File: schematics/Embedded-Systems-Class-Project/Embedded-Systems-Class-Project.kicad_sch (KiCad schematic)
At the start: 6 parts

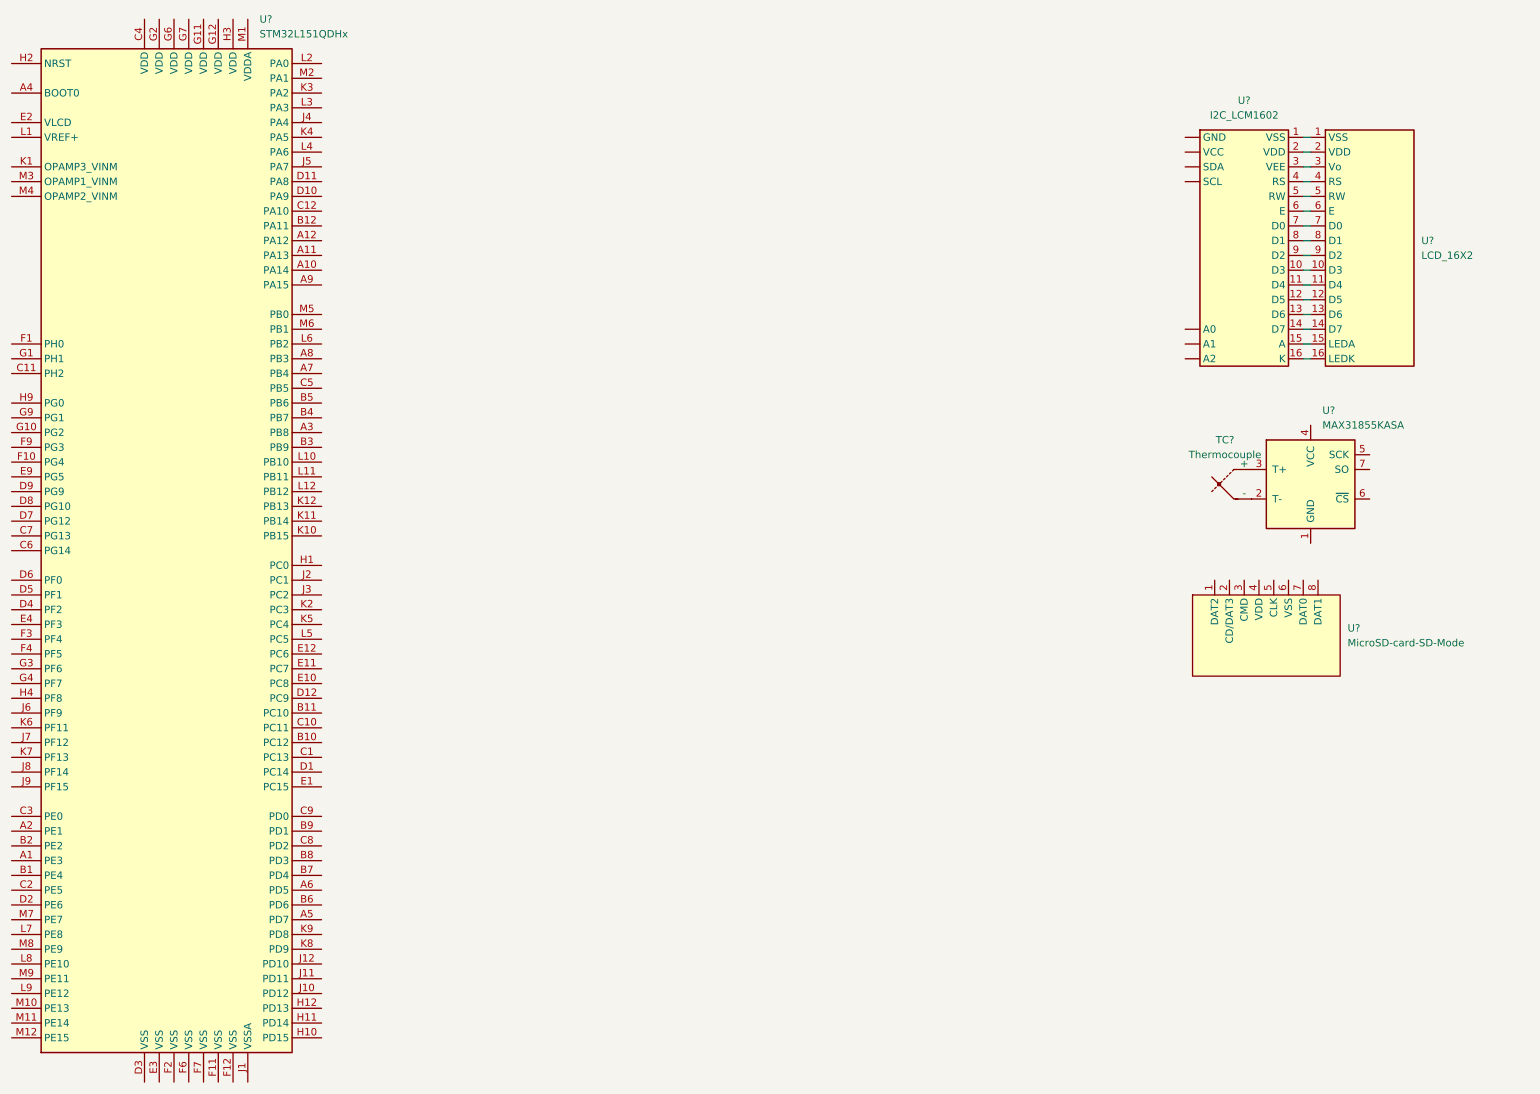
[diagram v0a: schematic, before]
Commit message: added connections to schematic
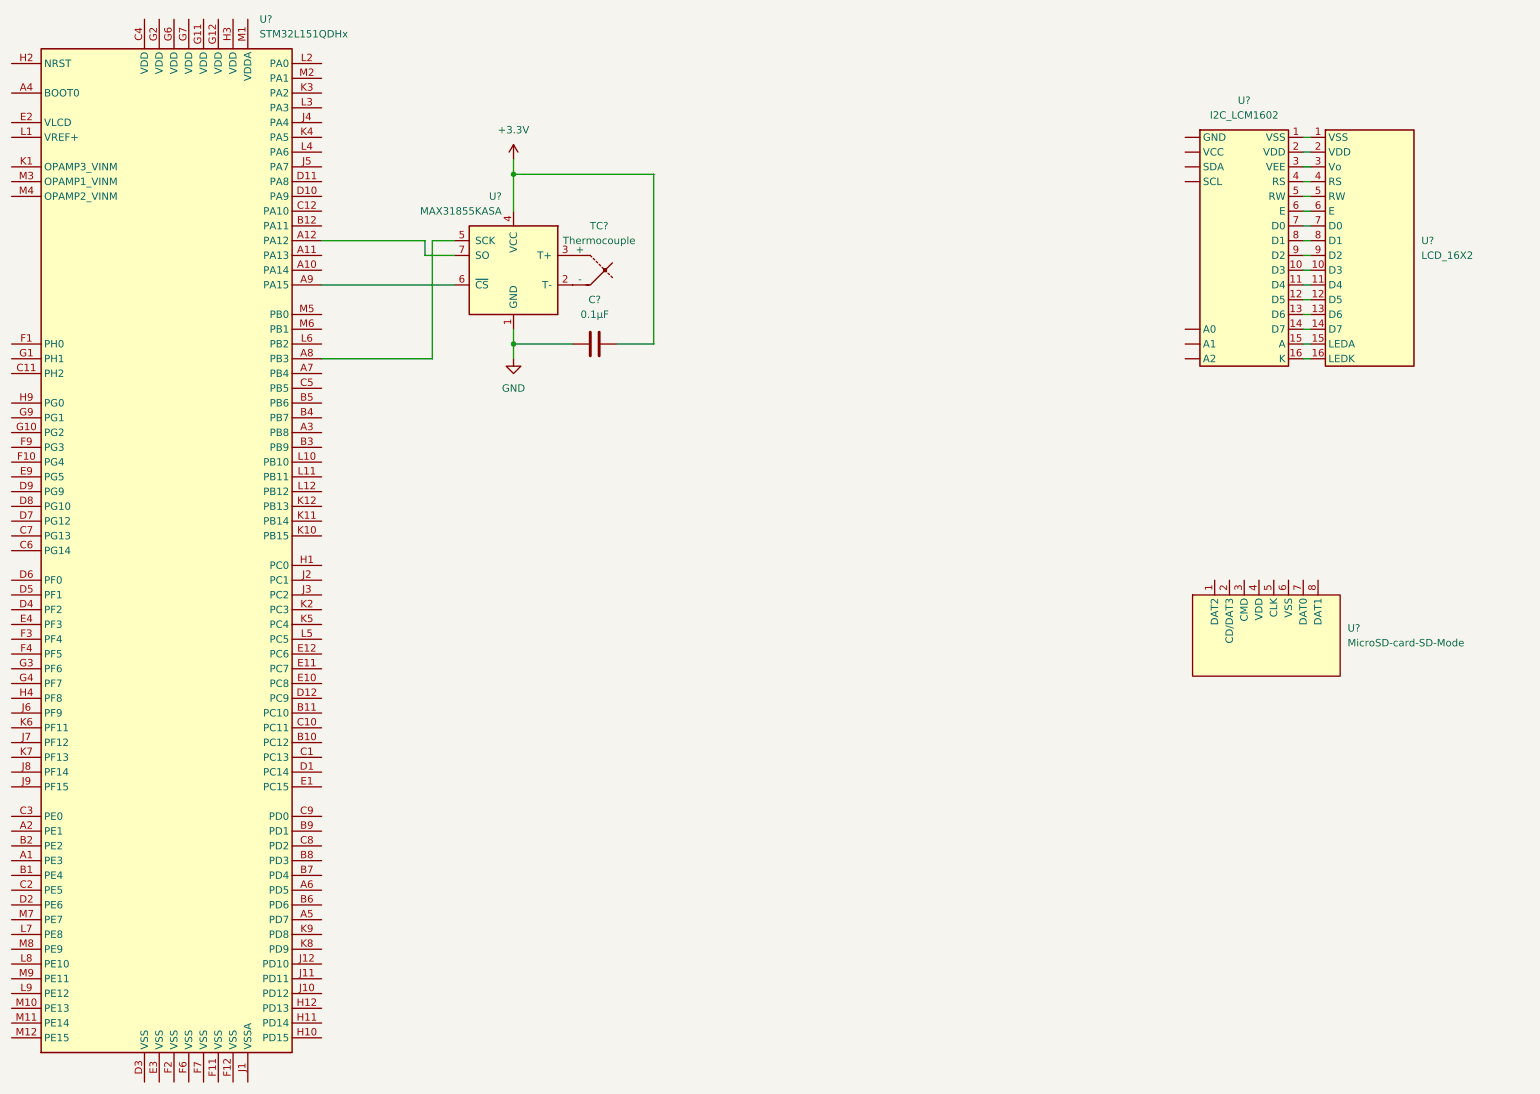
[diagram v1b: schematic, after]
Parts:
- added C?: 0.1μF, symbol Device:C
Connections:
- net GND: now reaches U?.1 (GND)
- net GND: now also C?.2
- net +3.3V: now reaches U?.4 (VCC)
- net +3.3V: now also C?.1
- net at U?.5 (SCK): now also U?.A8 (PB3)
- net at U?.6 (~{CS}): now also U?.A9 (PA15)
- net at U?.7 (SO): now also U?.A12 (PA12)
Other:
- moved on the sheet: TC?, U?
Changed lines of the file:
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@@
 (kicad_sch (version 20211123) (generator eeschema)
   (paper "A4")
+  (junction (at 107.95 39.37) (diameter 0) (color 0 0 0 0)
+  )
+  (junction (at 107.95 68.58) (diameter 0) (color 0 0 0 0)
+  )
+  (wire (pts (xy 74.93 58.42) (xy 97.79 58.42))
+    (stroke (width 0) (type default) (color 0 0 0 0))
+  )
   (wire (pts (xy 243.84 35.56) (xy 245.11 35.56))
     (stroke (width 0) (type default) (color 0 0 0 0))
   )
+  (wire (pts (xy 107.95 39.37) (xy 132.08 39.37))
+    (stroke (width 0) (type default) (color 0 0 0 0))
+  )
   (wire (pts (xy 243.84 63.5) (xy 245.11 63.5))
     (stroke (width 0) (type default) (color 0 0 0 0))
@@
     (stroke (width 0) (type default) (color 0 0 0 0))
   )
+  (wire (pts (xy 107.95 36.83) (xy 107.95 39.37))
+    (stroke (width 0) (type default) (color 0 0 0 0))
+  )
+  (wire (pts (xy 97.79 53.34) (xy 92.71 53.34))
+    (stroke (width 0) (type default) (color 0 0 0 0))
+  )
   (wire (pts (xy 243.84 60.96) (xy 245.11 60.96))
     (stroke (width 0) (type default) (color 0 0 0 0))
@@
     (stroke (width 0) (type default) (color 0 0 0 0))
   )
+  (wire (pts (xy 107.95 66.04) (xy 107.95 68.58))
+    (stroke (width 0) (type default) (color 0 0 0 0))
+  )
   (wire (pts (xy 243.84 58.42) (xy 245.11 58.42))
     (stroke (width 0) (type default) (color 0 0 0 0))
@@
     (stroke (width 0) (type default) (color 0 0 0 0))
   )
+  (wire (pts (xy 92.71 50.8) (xy 92.71 53.34))
+    (stroke (width 0) (type default) (color 0 0 0 0))
+  )
   (wire (pts (xy 243.84 33.02) (xy 245.11 33.02))
     (stroke (width 0) (type default) (color 0 0 0 0))
   )
+  (wire (pts (xy 107.95 68.58) (xy 107.95 71.12))
+    (stroke (width 0) (type default) (color 0 0 0 0))
+  )
+  (wire (pts (xy 74.93 71.12) (xy 93.98 71.12))
+    (stroke (width 0) (type default) (color 0 0 0 0))
+  )
+  (wire (pts (xy 107.95 68.58) (xy 118.11 68.58))
+    (stroke (width 0) (type default) (color 0 0 0 0))
+  )
+  (wire (pts (xy 107.95 45.72) (xy 107.95 39.37))
+    (stroke (width 0) (type default) (color 0 0 0 0))
+  )
+  (wire (pts (xy 132.08 39.37) (xy 132.08 68.58))
+    (stroke (width 0) (type default) (color 0 0 0 0))
+  )
+  (wire (pts (xy 74.93 50.8) (xy 92.71 50.8))
+    (stroke (width 0) (type default) (color 0 0 0 0))
+  )
+  (wire (pts (xy 125.73 68.58) (xy 132.08 68.58))
+    (stroke (width 0) (type default) (color 0 0 0 0))
+  )
   (wire (pts (xy 243.84 45.72) (xy 245.11 45.72))
     (stroke (width 0) (type default) (color 0 0 0 0))
   )
+  (wire (pts (xy 97.79 50.8) (xy 93.98 50.8))
+    (stroke (width 0) (type default) (color 0 0 0 0))
+  )
   (wire (pts (xy 243.84 66.04) (xy 245.11 66.04))
     (stroke (width 0) (type default) (color 0 0 0 0))
   )
+  (wire (pts (xy 93.98 50.8) (xy 93.98 71.12))
+    (stroke (width 0) (type default) (color 0 0 0 0))
+  )
   (wire (pts (xy 243.84 38.1) (xy 245.11 38.1))
     (stroke (width 0) (type default) (color 0 0 0 0))
@@
     (stroke (width 0) (type default) (color 0 0 0 0))
   )
-  (symbol (lib_id "Device:Thermocouple") (at 232.41 92.71 0) (unit 1)
-    (in_bom yes) (on_board yes) (fields_autoplaced)
-    (property "Reference" "TC?" (id 0) (at 230.378 85.09 0))
-    (property "Value" "Thermocouple" (id 1) (at 230.378 87.63 0))
-    (property "Footprint" "" (id 2) (at 217.805 91.44 0)
-      (effects (font (size 1.27 1.27)) hide)
-    )
-    (property "Datasheet" "~" (id 3) (at 217.805 91.44 0)
+  (symbol (lib_id "Device:Thermocouple") (at 120.65 55.88 0) (mirror y) (unit 1)
+    (in_bom yes) (on_board yes) (fields_autoplaced)
+    (property "Reference" "TC?" (id 0) (at 122.682 48.26 0))
+    (property "Value" "Thermocouple" (id 1) (at 122.682 50.8 0))
+    (property "Footprint" "" (id 2) (at 135.255 54.61 0)
+      (effects (font (size 1.27 1.27)) hide)
+    )
+    (property "Datasheet" "~" (id 3) (at 135.255 54.61 0)
+      (effects (font (size 1.27 1.27)) hide)
+    )
+    (pin "1")
+    (pin "2")
+  )
+  (symbol (lib_id "power:+3.3V") (at 107.95 36.83 0) (unit 1)
+    (in_bom yes) (on_board yes) (fields_autoplaced)
+    (property "Reference" "#PWR?" (id 0) (at 107.95 40.64 0)
+      (effects (font (size 1.27 1.27)) hide)
+    )
+    (property "Value" "+3.3V" (id 1) (at 107.95 31.75 0))
+    (property "Footprint" "" (id 2) (at 107.95 36.83 0)
+      (effects (font (size 1.27 1.27)) hide)
+    )
+    (property "Datasheet" "" (id 3) (at 107.95 36.83 0)
+      (effects (font (size 1.27 1.27)) hide)
+    )
+    (pin "1")
+  )
+  (symbol (lib_id "Device:C") (at 121.92 68.58 270) (unit 1)
+    (in_bom yes) (on_board yes) (fields_autoplaced)
+    (property "Reference" "C?" (id 0) (at 121.92 60.96 90))
+    (property "Value" "0.1μF" (id 1) (at 121.92 63.5 90))
+    (property "Footprint" "" (id 2) (at 118.11 69.5452 0)
+      (effects (font (size 1.27 1.27)) hide)
+    )
+    (property "Datasheet" "~" (id 3) (at 121.92 68.58 0)
       (effects (font (size 1.27 1.27)) hide)
     )
@@
     (pin "9")
   )
-  (symbol (lib_id "Sensor_Temperature:MAX31855KASA") (at 245.11 92.71 0) (unit 1)
-    (in_bom yes) (on_board yes) (fields_autoplaced)
-    (property "Reference" "U?" (id 0) (at 247.1294 80.01 0)
-      (effects (font (size 1.27 1.27)) (justify left))
-    )
-    (property "Value" "MAX31855KASA" (id 1) (at 247.1294 82.55 0)
-      (effects (font (size 1.27 1.27)) (justify left))
-    )
-    (property "Footprint" "Package_SO:SOIC-8_3.9x4.9mm_P1.27mm" (id 2) (at 270.51 101.6 0)
+  (symbol (lib_id "Sensor_Temperature:MAX31855KASA") (at 107.95 55.88 0) (mirror y) (unit 1)
+    (in_bom yes) (on_board yes) (fields_autoplaced)
+    (property "Reference" "U?" (id 0) (at 105.9306 43.18 0)
+      (effects (font (size 1.27 1.27)) (justify left))
+    )
+    (property "Value" "MAX31855KASA" (id 1) (at 105.9306 45.72 0)
+      (effects (font (size 1.27 1.27)) (justify left))
+    )
+    (property "Footprint" "Package_SO:SOIC-8_3.9x4.9mm_P1.27mm" (id 2) (at 82.55 64.77 0)
       (effects (font (size 1.27 1.27) italic) hide)
     )
-    (property "Datasheet" "http://datasheets.maximintegrated.com/en/ds/MAX31855.pdf" (id 3) (at 245.11 92.71 0)
+    (property "Datasheet" "http://datasheets.maximintegrated.com/en/ds/MAX31855.pdf" (id 3) (at 107.95 55.88 0)
       (effects (font (size 1.27 1.27)) hide)
     )
@@
     (pin "9")
   )
+  (symbol (lib_id "power:GND") (at 107.95 71.12 0) (unit 1)
+    (in_bom yes) (on_board yes) (fields_autoplaced)
+    (property "Reference" "#PWR?" (id 0) (at 107.95 77.47 0)
+      (effects (font (size 1.27 1.27)) hide)
+    )
+    (property "Value" "GND" (id 1) (at 107.95 76.2 0))
+    (property "Footprint" "" (id 2) (at 107.95 71.12 0)
+      (effects (font (size 1.27 1.27)) hide)
+    )
+    (property "Datasheet" "" (id 3) (at 107.95 71.12 0)
+      (effects (font (size 1.27 1.27)) hide)
+    )
+    (pin "1")
+  )
   (sheet_instances
     (path "/" (page "1"))
   )
   (symbol_instances
+    (path "/1f83a5fa-bf85-444a-be10-8f0bc87b40cd"
+      (reference "#PWR?") (unit 1) (value "+3.3V") (footprint "")
+    )
+    (path "/f1dcfb07-bcfe-4f3d-9507-6c63394d8b8a"
+      (reference "#PWR?") (unit 1) (value "GND") (footprint "")
+    )
+    (path "/37f3e6f4-a15f-471f-8eb9-d57efc4b3394"
+      (reference "C?") (unit 1) (value "0.1μF") (footprint "")
+    )
     (path "/102c21df-c231-4030-8d1c-907ec73ab494"
       (reference "TC?") (unit 1) (value "Thermocouple") (footprint "")

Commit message: added additional thermocouples and converters
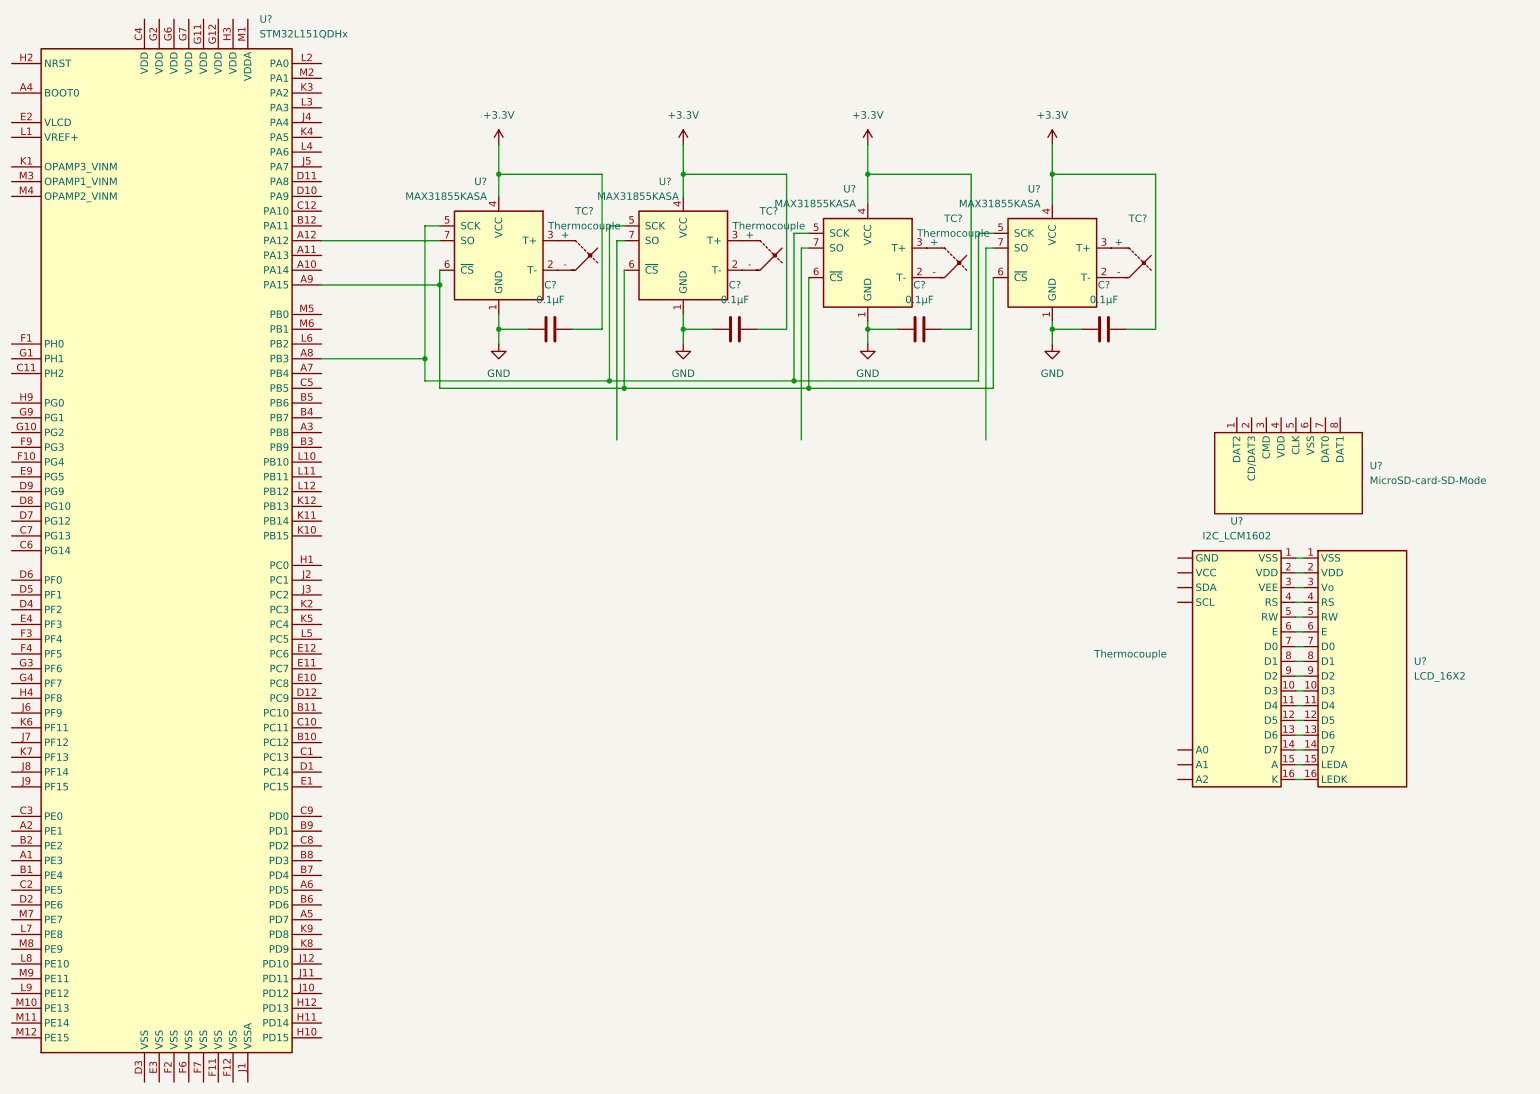
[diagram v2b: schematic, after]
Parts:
- added C? (x3): 0.1μF, symbol Device:C
- added TC? (x3): Thermocouple, symbol Device:Thermocouple
- added U? (x3): MAX31855KASA, Package_SO:SOIC-8_3.9x4.9mm_P1.27mm, symbol Sensor_Temperature:MAX31855KASA
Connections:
- net +3.3V: now also C?.1, C?.1, C?.1, U?.4 (VCC), U?.4 (VCC), U?.4 (VCC)
- net GND: now also C?.2, C?.2, C?.2, U?.1 (GND), U?.1 (GND), U?.1 (GND)
- net at U?.5 (SCK), U?.A8 (PB3): now also U?.5 (SCK), U?.5 (SCK), U?.5 (SCK)
- net at U?.6 (~{CS}), U?.A9 (PA15): now also U?.6 (~{CS}), U?.6 (~{CS}), U?.6 (~{CS})
- new net: TC?.1 (+), U?.3 (T+) (x3)
- new net: TC?.2 (-), U?.2 (T-) (x3)
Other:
- moved on the sheet: C?, TC?, U?

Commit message: updated schematic and library
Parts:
- removed C?: 0.1μF, symbol Device:C
- removed TC?: Thermocouple, symbol Device:Thermocouple
- removed U?: MAX31855KASA, Package_SO:SOIC-8_3.9x4.9mm_P1.27mm, symbol Sensor_Temperature:MAX31855KASA
- added U?: SC18IS606, symbol Embedded-Systems-Class-Project:SC18IS606
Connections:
- net +3.3V: now also U?.12 (VDD)
- net GND: now also U?.13 (VSS)
- net at U?.5 (SCK), U?.5 (SCK), U?.5 (SCK): now also U?.11 (SPICLK); no longer U?.A8 (PB3)
- net at U?.7 (SO): now also U?.7 (SO), U?.7 (SO), U?.14 (MISO)
- net at U?.A12 (PA12): no longer U?.7 (SO)
- net at U?.A3 (PB8): now also U?.2 (SCL)
- net OUT: now reaches U?.B3 (PB9)
- net OUT: now also U?.1 (SDA)
- new net: U?.16 (SS1), U?.6 (~{CS})
- new net: U?.6 (~{CS}), U?.8 (SS2)
- new net: U?.6 (~{CS}), U?.9 (SS0)
- now unconnected: U?.A9 (PA15)
- no-connect marks 0 -> 2
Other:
- moved on the sheet: C?, TC?, U?
